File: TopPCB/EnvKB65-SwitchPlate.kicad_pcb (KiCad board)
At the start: 2 copper layers, 320.8 x 99.3 mm, 6 parts

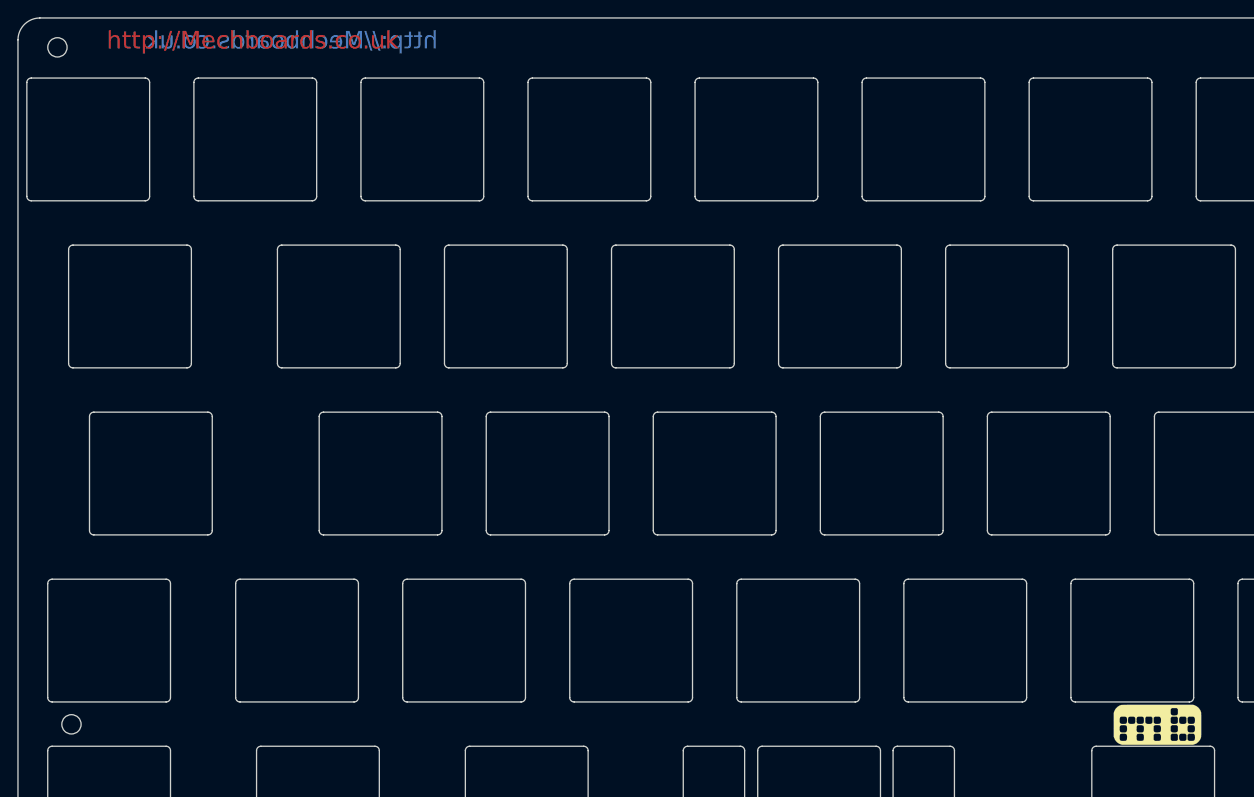
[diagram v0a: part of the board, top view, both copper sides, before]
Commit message: Swapped out mechboads logo for personal order
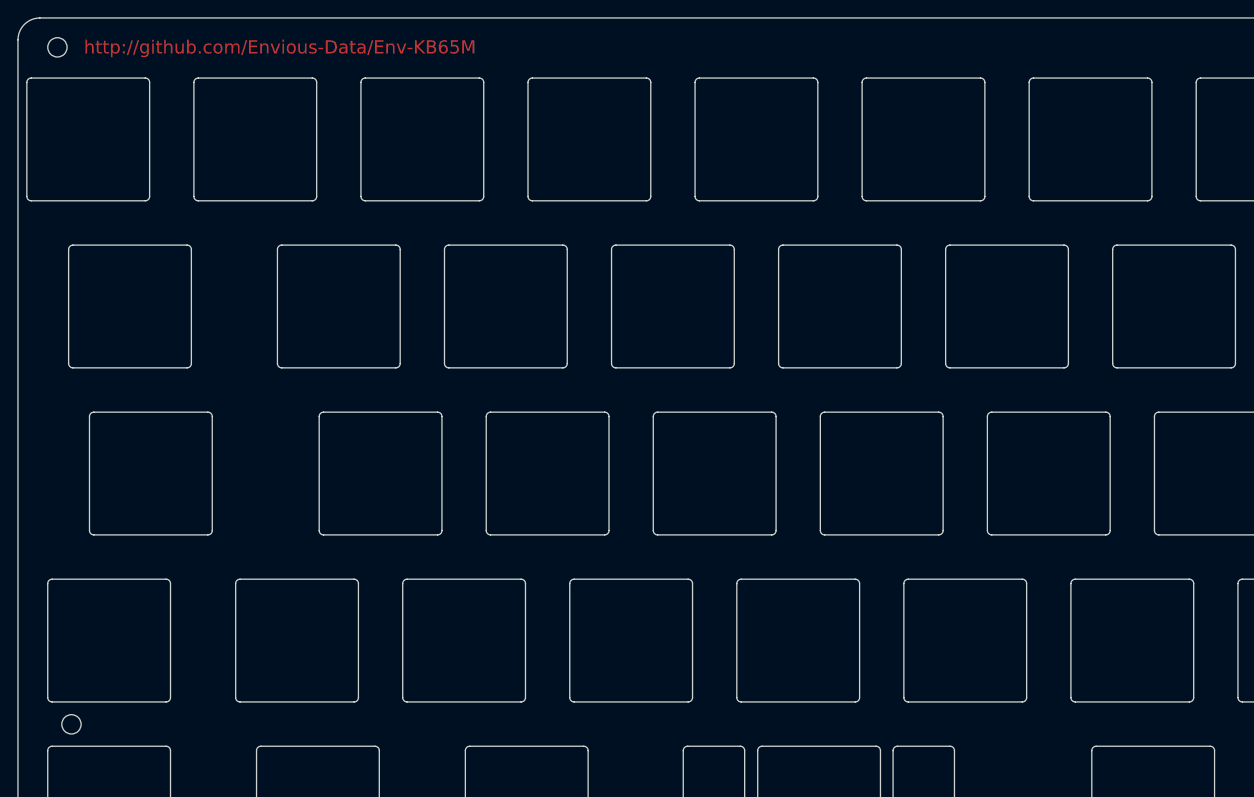
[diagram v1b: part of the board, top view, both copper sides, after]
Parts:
- removed Ref**: Val**, MechboardsLogo:mechboardsLOGO_10mm
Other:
- board text added: "http://github.com/Envious-Data/Env-KB65M"
- board text removed: "http://Mechboards.co.uk"

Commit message: Added ANSI support, generated Gerbers and sent to JLCPCB
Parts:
- removed H6: MountingHole, MountingHole:MountingHole_2.2mm_M2
- added H1: MountingHole, MountingHole:MountingHole_2.2mm_M2, F.Cu at (69.0, 101.0)
- moved H3 297.2 mm to (367.8, 180.5)
- moved H4 154.1 mm to (225.0, 122.5)
- moved H2 86.1 mm to (86.8, 185.2)
- moved H5 55.9 mm to (231.3, 178.0)
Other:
- outline, holes or cut-outs redrawn

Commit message: Embiggened the PCB to allow for 4mm edge spaces to comply with JLCPCB
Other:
- board size 320.8 x 99.3 mm -> 326.8 x 101 mm
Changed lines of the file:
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@@
   (general
     (thickness 1.6)
-    (drawings 659)
+    (drawings 665)
     (tracks 0)
     (zones 0)
@@
     (pad_to_mask_clearance 0)
     (aux_axis_origin 0 0)
-    (grid_origin 342.83125 155.453)
+    (grid_origin 384.3125 175.15)
     (visible_elements 7FFFFFFF)
     (pcbplotparams
       (layerselection 0x010fc_ffffffff)
-      (usegerberextensions false)
+      (usegerberextensions true)
       (usegerberattributes false)
       (usegerberadvancedattributes false)
@@
       (plotinvisibletext false)
       (padsonsilk false)
-      (subtractmaskfromsilk false)
+      (subtractmaskfromsilk true)
       (outputformat 1)
       (mirror false)
@@
     )
     (pad 1 np_thru_hole circle (at 0 0) (size 2.2 2.2) (drill 2.2) (layers *.Cu *.Mask))
+  )
+  (dimension 4 (width 0.12) (layer Dwgs.User)
+    (gr_text "4.000 mm" (at 385.4575 196.7 270) (layer Dwgs.User)
+      (effects (font (size 1 1) (thickness 0.15)))
+    )
+    (feature1 (pts (xy 383.2375 198.7) (xy 384.773921 198.7)))
+    (feature2 (pts (xy 383.2375 194.7) (xy 384.773921 194.7)))
+    (crossbar (pts (xy 384.1875 194.7) (xy 384.1875 198.7)))
+    (arrow1a (pts (xy 384.1875 198.7) (xy 383.601079 197.573496)))
+    (arrow1b (pts (xy 384.1875 198.7) (xy 384.773921 197.573496)))
+    (arrow2a (pts (xy 384.1875 194.7) (xy 383.601079 195.826504)))
+    (arrow2b (pts (xy 384.1875 194.7) (xy 384.773921 195.826504)))
+  )
+  (dimension 4 (width 0.12) (layer Dwgs.User)
+    (gr_text "4.000 mm" (at 81.3325 196.7 270) (layer Dwgs.User)
+      (effects (font (size 1 1) (thickness 0.15)))
+    )
+    (feature1 (pts (xy 78.6375 198.7) (xy 80.648921 198.7)))
+    (feature2 (pts (xy 78.6375 194.7) (xy 80.648921 194.7)))
+    (crossbar (pts (xy 80.0625 194.7) (xy 80.0625 198.7)))
+    (arrow1a (pts (xy 80.0625 198.7) (xy 79.476079 197.573496)))
+    (arrow1b (pts (xy 80.0625 198.7) (xy 80.648921 197.573496)))
+    (arrow2a (pts (xy 80.0625 194.7) (xy 79.476079 195.826504)))
+    (arrow2b (pts (xy 80.0625 194.7) (xy 80.648921 195.826504)))
+  )
+  (dimension 4 (width 0.12) (layer Dwgs.User)
+    (gr_text "4.000 mm" (at 63.5125 108.43) (layer Dwgs.User)
+      (effects (font (size 1 1) (thickness 0.15)))
+    )
+    (feature1 (pts (xy 61.5125 110.2) (xy 61.5125 109.113579)))
+    (feature2 (pts (xy 65.5125 110.2) (xy 65.5125 109.113579)))
+    (crossbar (pts (xy 65.5125 109.7) (xy 61.5125 109.7)))
+    (arrow1a (pts (xy 61.5125 109.7) (xy 62.639004 109.113579)))
+    (arrow1b (pts (xy 61.5125 109.7) (xy 62.639004 110.286421)))
+    (arrow2a (pts (xy 65.5125 109.7) (xy 64.385996 109.113579)))
+    (arrow2b (pts (xy 65.5125 109.7) (xy 64.385996 110.286421)))
+  )
+  (dimension 4 (width 0.12) (layer Dwgs.User)
+    (gr_text "4.000 mm" (at 330.4425 102.5 90) (layer Dwgs.User)
+      (effects (font (size 1 1) (thickness 0.15)))
+    )
+    (feature1 (pts (xy 332.8125 100.5) (xy 331.126079 100.5)))
+    (feature2 (pts (xy 332.8125 104.5) (xy 331.126079 104.5)))
+    (crossbar (pts (xy 331.7125 104.5) (xy 331.7125 100.5)))
+    (arrow1a (pts (xy 331.7125 100.5) (xy 332.298921 101.626504)))
+    (arrow1b (pts (xy 331.7125 100.5) (xy 331.126079 101.626504)))
+    (arrow2a (pts (xy 331.7125 104.5) (xy 332.298921 103.373496)))
+    (arrow2b (pts (xy 331.7125 104.5) (xy 331.126079 103.373496)))
+  )
+  (dimension 4 (width 0.12) (layer Dwgs.User)
+    (gr_text "4.000 mm" (at 377.952014 159.65 90) (layer Dwgs.User)
+      (effects (font (size 1 1) (thickness 0.15)))
+    )
+    (feature1 (pts (xy 380.0125 157.65) (xy 378.635593 157.65)))
+    (feature2 (pts (xy 380.0125 161.65) (xy 378.635593 161.65)))
+    (crossbar (pts (xy 379.222014 161.65) (xy 379.222014 157.65)))
+    (arrow1a (pts (xy 379.222014 157.65) (xy 379.808435 158.776504)))
+    (arrow1b (pts (xy 379.222014 157.65) (xy 378.635593 158.776504)))
+    (arrow2a (pts (xy 379.222014 161.65) (xy 379.808435 160.523496)))
+    (arrow2b (pts (xy 379.222014 161.65) (xy 378.635593 160.523496)))
+  )
+  (dimension 4 (width 0.12) (layer Dwgs.User)
+    (gr_text "4.000 mm" (at 386.3125 160.58) (layer Dwgs.User)
+      (effects (font (size 1 1) (thickness 0.15)))
+    )
+    (feature1 (pts (xy 388.3125 162.875) (xy 388.3125 161.263579)))
+    (feature2 (pts (xy 384.3125 162.875) (xy 384.3125 161.263579)))
+    (crossbar (pts (xy 384.3125 161.85) (xy 388.3125 161.85)))
+    (arrow1a (pts (xy 388.3125 161.85) (xy 387.185996 162.436421)))
+    (arrow1b (pts (xy 388.3125 161.85) (xy 387.185996 161.263579)))
+    (arrow2a (pts (xy 384.3125 161.85) (xy 385.439004 162.436421)))
+    (arrow2b (pts (xy 384.3125 161.85) (xy 385.439004 161.263579)))
   )
   (gr_line (start 343.33125 133.07906) (end 341.935 133.07906) (layer Edge.Cuts) (width 0.1))
@@
   )
   (gr_arc (start 350.025 100.15) (end 352.525 100.15) (angle -90) (layer Edge.Cuts) (width 0.1))
-  (gr_line (start 352.525 156.95) (end 352.525 100.15) (layer Edge.Cuts) (width 0.1))
-  (gr_arc (start 355.025 156.95) (end 352.525 156.95) (angle -90) (layer Edge.Cuts) (width 0.1))
-  (gr_line (start 382.8 159.45) (end 355.025 159.45) (layer Edge.Cuts) (width 0.1))
-  (gr_arc (start 382.8 161.95) (end 385.3 161.95) (angle -90) (layer Edge.Cuts) (width 0.1))
+  (gr_line (start 352.525 155.15) (end 352.525 100.15) (layer Edge.Cuts) (width 0.1))
+  (gr_arc (start 355.025 155.15) (end 352.525 155.15) (angle -90) (layer Edge.Cuts) (width 0.1))
+  (gr_line (start 385.8125 157.65) (end 355.025 157.65) (layer Edge.Cuts) (width 0.1))
+  (gr_arc (start 385.8125 160.15) (end 388.3125 160.15) (angle -90) (layer Edge.Cuts) (width 0.1))
   (gr_line (start 384.3125 181.2) (end 384.3125 194.2) (layer Edge.Cuts) (width 0.1))
   (gr_arc (start 351.7625 181.2) (end 351.7625 180.7) (angle -90) (layer Edge.Cuts) (width 0.1))
@@
   (gr_line (start 189.05 143.1) (end 189.05 156.1) (layer Edge.Cuts) (width 0.1))
   (gr_line (start 175.55 142.6) (end 188.55 142.6) (layer Edge.Cuts) (width 0.1))
-  (gr_arc (start 67 194.45) (end 64.5 194.45) (angle -90) (layer Edge.Cuts) (width 0.1))
-  (gr_arc (start 382.8 194.45) (end 382.8 196.95) (angle -90) (layer Edge.Cuts) (width 0.1))
-  (gr_arc (start 67 100.15) (end 67 97.65) (angle -90) (layer Edge.Cuts) (width 0.1))
-  (gr_line (start 64.5 194.45) (end 64.5 100.15) (layer Edge.Cuts) (width 0.1))
-  (gr_line (start 67 196.95) (end 382.8 196.95) (layer Edge.Cuts) (width 0.1))
-  (gr_line (start 385.3 194.45) (end 385.3 161.95) (layer Edge.Cuts) (width 0.1))
-  (gr_line (start 350.025 97.65) (end 67 97.65) (layer Edge.Cuts) (width 0.1))
+  (gr_arc (start 64.0125 196.2) (end 61.5125 196.2) (angle -90) (layer Edge.Cuts) (width 0.1))
+  (gr_arc (start 385.8125 196.2) (end 385.8125 198.7) (angle -90) (layer Edge.Cuts) (width 0.1))
+  (gr_arc (start 64.0125 100.15) (end 64.0125 97.65) (angle -90) (layer Edge.Cuts) (width 0.1))
+  (gr_line (start 61.5125 196.2) (end 61.5125 100.15) (layer Edge.Cuts) (width 0.1))
+  (gr_line (start 64.0125 198.7) (end 385.8125 198.7) (layer Edge.Cuts) (width 0.1))
+  (gr_line (start 388.3125 196.2) (end 388.3125 160.15) (layer Edge.Cuts) (width 0.1))
+  (gr_line (start 350.025 97.65) (end 64.0125 97.65) (layer Edge.Cuts) (width 0.1))
 )

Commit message: Mount hole tweak to allow for switches to seat properly with a spacer installed
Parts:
- added H2: MountingHole, MountingHole:MountingHole_2.2mm_M2, F.Cu at (69.0, 101.0)
- added H3: MountingHole, MountingHole:MountingHole_2.2mm_M2, F.Cu at (86.8, 185.2)
- added H5: MountingHole, MountingHole:MountingHole_2.2mm_M2, F.Cu at (224.9, 121.8)
- added H6: MountingHole, MountingHole:MountingHole_2.2mm_M2, F.Cu at (210.6, 184.5)
- moved H4 154.1 mm to (367.8, 180.5)
- moved H6 21.6 mm to (210.6, 184.5)
- renumbered H1 to H2, H2 to H3, H3 to H4, H5 to H6

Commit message: moved some mount holes a tiny bit and adjusted some traces for wider clearance.
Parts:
- removed the H2 at (69.0, 101.0)
- removed the H3 at (86.8, 185.2)
- removed the H6 at (210.6, 184.5)
- moved H4 2.30 mm to (367.8, 178.2) (x2)
- moved H5 0.23 mm to (224.9, 121.6)
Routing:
- added copper zone on B.Cu, net (none)
- added copper zone on F.Cu, net (none)

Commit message: moved mount hole#6 up by 1mm and changed stabilizer cut out.
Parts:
- moved H6 2.50 mm to (210.6, 182.0)
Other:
- outline, holes or cut-outs redrawn

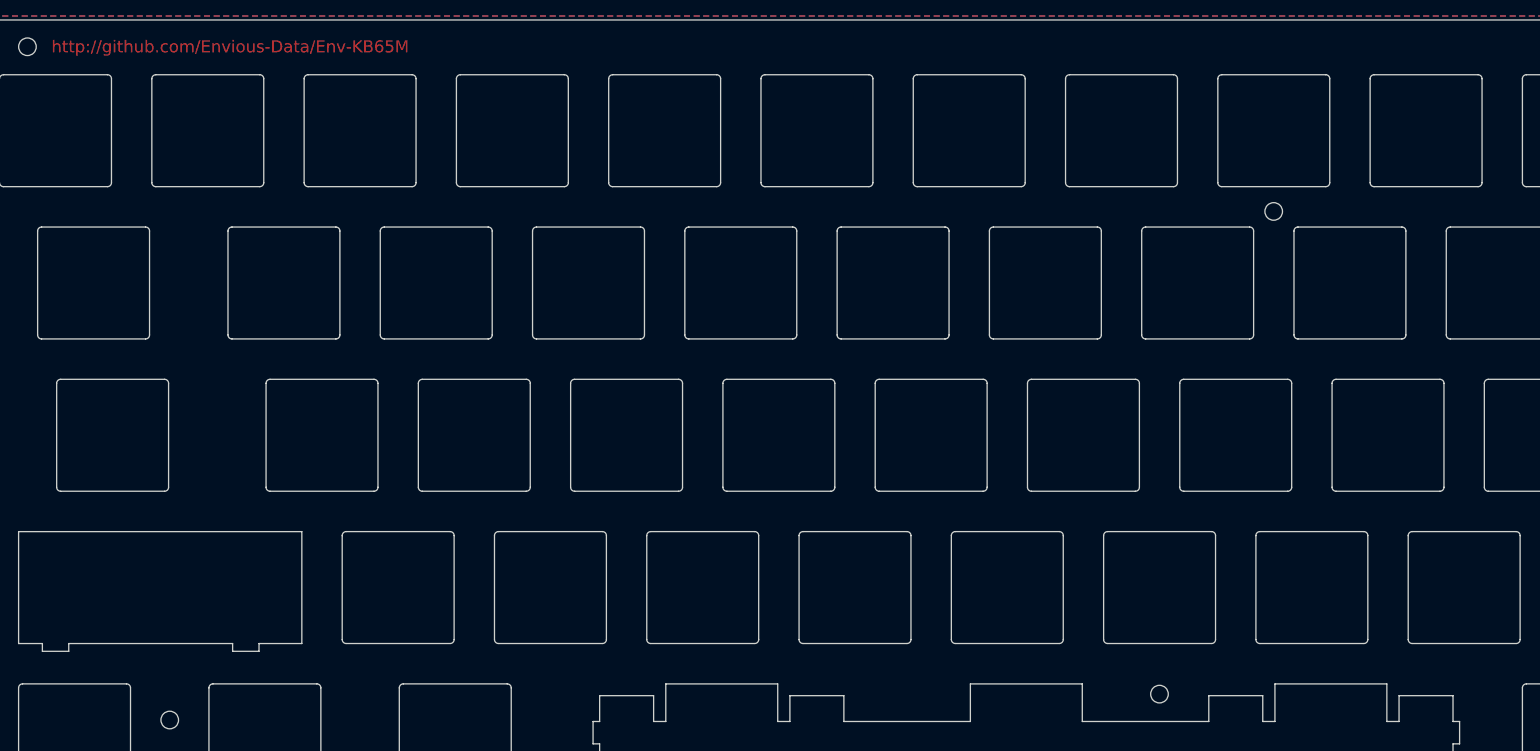
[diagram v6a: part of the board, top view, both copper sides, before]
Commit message: moved mount hole "H5" to the right by 40.5mm on all PCBs
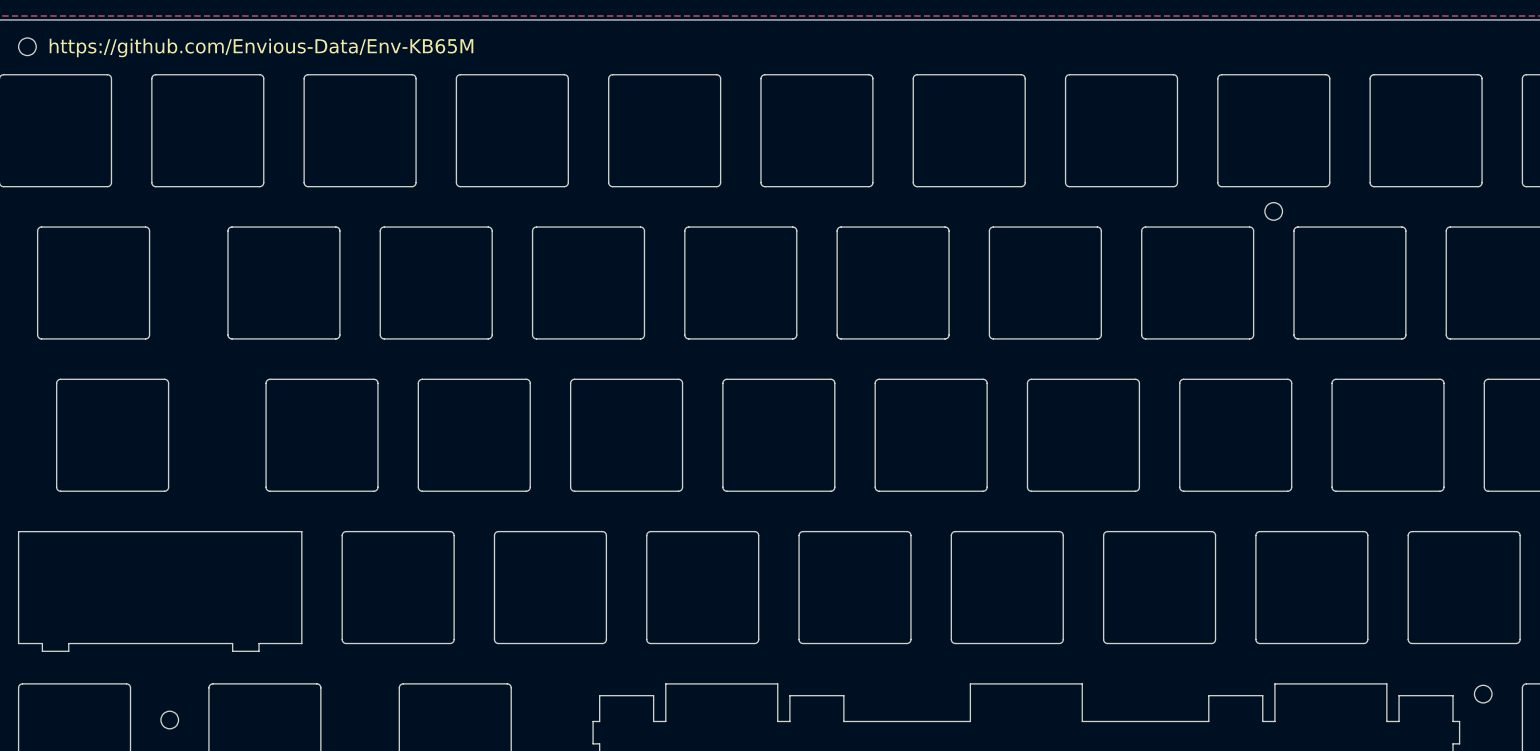
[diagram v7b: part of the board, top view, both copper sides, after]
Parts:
- moved H6 40.5 mm to (251.1, 182.0)
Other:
- board text added: "https://github.com/Envious-Data/Env-KB65M"
- board text removed: "http://github.com/Envious-Data/Env-KB65M"
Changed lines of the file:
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@@
       (effects (font (size 1 1) (thickness 0.15)))
     )
-    (fp_circle (center 0 0) (end 2.45 0) (layer F.CrtYd) (width 0.05))
-    (fp_circle (center 0 0) (end 2.2 0) (layer Cmts.User) (width 0.15))
-    (fp_text user %R (at 0.3 0) (layer F.Fab)
-      (effects (font (size 1 1) (thickness 0.15)))
-    )
-    (pad 1 np_thru_hole circle (at 0 0) (size 2.2 2.2) (drill 2.2) (layers *.Cu *.Mask))
-  )
-  (module MountingHole:MountingHole_2.2mm_M2 (layer F.Cu)
-    (at 210.6125 181.98)
+    (fp_circle (center 0 0) (end 2.2 0) (layer Cmts.User) (width 0.15))
+    (fp_circle (center 0 0) (end 2.45 0) (layer F.CrtYd) (width 0.05))
+    (fp_text user %R (at 0.3 0) (layer F.Fab)
+      (effects (font (size 1 1) (thickness 0.15)))
+    )
+    (pad 1 np_thru_hole circle (at 0 0) (size 2.2 2.2) (drill 2.2) (layers *.Cu *.Mask))
+  )
+  (module MountingHole:MountingHole_2.2mm_M2 (layer F.Cu)
+    (at 251.1125 181.98)
     (descr "Mounting Hole 2.2mm, no annular, M2")
     (tags "mounting hole 2.2mm no annular m2")
@@
       (effects (font (size 1 1) (thickness 0.15)))
     )
-    (fp_circle (center 0 0) (end 2.45 0) (layer F.CrtYd) (width 0.05))
-    (fp_circle (center 0 0) (end 2.2 0) (layer Cmts.User) (width 0.15))
+    (fp_circle (center 0 0) (end 2.2 0) (layer Cmts.User) (width 0.15))
+    (fp_circle (center 0 0) (end 2.45 0) (layer F.CrtYd) (width 0.05))
     (fp_text user %R (at 0.3 0) (layer F.Fab)
       (effects (font (size 1 1) (thickness 0.15)))
@@
       (effects (font (size 1 1) (thickness 0.15)))
     )
-    (fp_circle (center 0 0) (end 2.45 0) (layer F.CrtYd) (width 0.05))
-    (fp_circle (center 0 0) (end 2.2 0) (layer Cmts.User) (width 0.15))
+    (fp_circle (center 0 0) (end 2.2 0) (layer Cmts.User) (width 0.15))
+    (fp_circle (center 0 0) (end 2.45 0) (layer F.CrtYd) (width 0.05))
     (fp_text user %R (at 0.225 -0.25) (layer F.Fab)
       (effects (font (size 1 1) (thickness 0.15)))
@@
       (effects (font (size 1 1) (thickness 0.15)))
     )
-    (fp_circle (center 0 0) (end 2.45 0) (layer F.CrtYd) (width 0.05))
-    (fp_circle (center 0 0) (end 2.2 0) (layer Cmts.User) (width 0.15))
+    (fp_circle (center 0 0) (end 2.2 0) (layer Cmts.User) (width 0.15))
+    (fp_circle (center 0 0) (end 2.45 0) (layer F.CrtYd) (width 0.05))
     (fp_text user %R (at 0.3 0) (layer F.Fab)
       (effects (font (size 1 1) (thickness 0.15)))
@@
       (effects (font (size 1 1) (thickness 0.15)))
     )
-    (fp_circle (center 0 0) (end 2.45 0) (layer F.CrtYd) (width 0.05))
-    (fp_circle (center 0 0) (end 2.2 0) (layer Cmts.User) (width 0.15))
+    (fp_circle (center 0 0) (end 2.2 0) (layer Cmts.User) (width 0.15))
+    (fp_circle (center 0 0) (end 2.45 0) (layer F.CrtYd) (width 0.05))
     (fp_text user %R (at 0.3 0) (layer F.Fab)
       (effects (font (size 1 1) (thickness 0.15)))
@@
       (effects (font (size 1 1) (thickness 0.15)))
     )
-    (fp_circle (center 0 0) (end 2.45 0) (layer F.CrtYd) (width 0.05))
-    (fp_circle (center 0 0) (end 2.2 0) (layer Cmts.User) (width 0.15))
-    (fp_text user %R (at 0.3 0) (layer F.Fab)
-      (effects (font (size 1 1) (thickness 0.15)))
-    )
-    (pad 1 np_thru_hole circle (at 0 0) (size 2.2 2.2) (drill 2.2) (layers *.Cu *.Mask))
+    (fp_circle (center 0 0) (end 2.2 0) (layer Cmts.User) (width 0.15))
+    (fp_circle (center 0 0) (end 2.45 0) (layer F.CrtYd) (width 0.05))
+    (fp_text user %R (at 0.3 0) (layer F.Fab)
+      (effects (font (size 1 1) (thickness 0.15)))
+    )
+    (pad 1 np_thru_hole circle (at 0 0) (size 2.2 2.2) (drill 2.2) (layers *.Cu *.Mask))
+  )
+  (gr_text https://github.com/Envious-Data/Env-KB65M (at 71.5675 101.0008) (layer F.SilkS)
+    (effects (font (size 1.75 1.75) (thickness 0.2)) (justify left))
   )
   (gr_line (start 341.45 124.8038) (end 341.45 123.5539) (layer Edge.Cuts) (width 0.1))
@@
   )
   (gr_line (start 64.5 100.15) (end 64.71125 100.15) (layer Dwgs.User) (width 0.01))
-  (gr_text http://github.com/Envious-Data/Env-KB65M (at 72 101) (layer F.Cu)
-    (effects (font (size 1.5 1.5) (thickness 0.2)) (justify left))
-  )
   (dimension 16.45 (width 0.12) (layer Dwgs.User)
     (gr_text "16.450 mm" (at 364.18 188.725 270) (layer Dwgs.User)
